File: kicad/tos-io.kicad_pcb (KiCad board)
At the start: 2 copper layers, 87.3 x 42.5 mm, 26 parts, among them J1 RaspPi Pin Header, J2 DE9_Receptacle, J3 Keyboard, J4 Mouse, J5 Conn_02x06_Odd_Even, SW1 STATUS, U1 MAX232

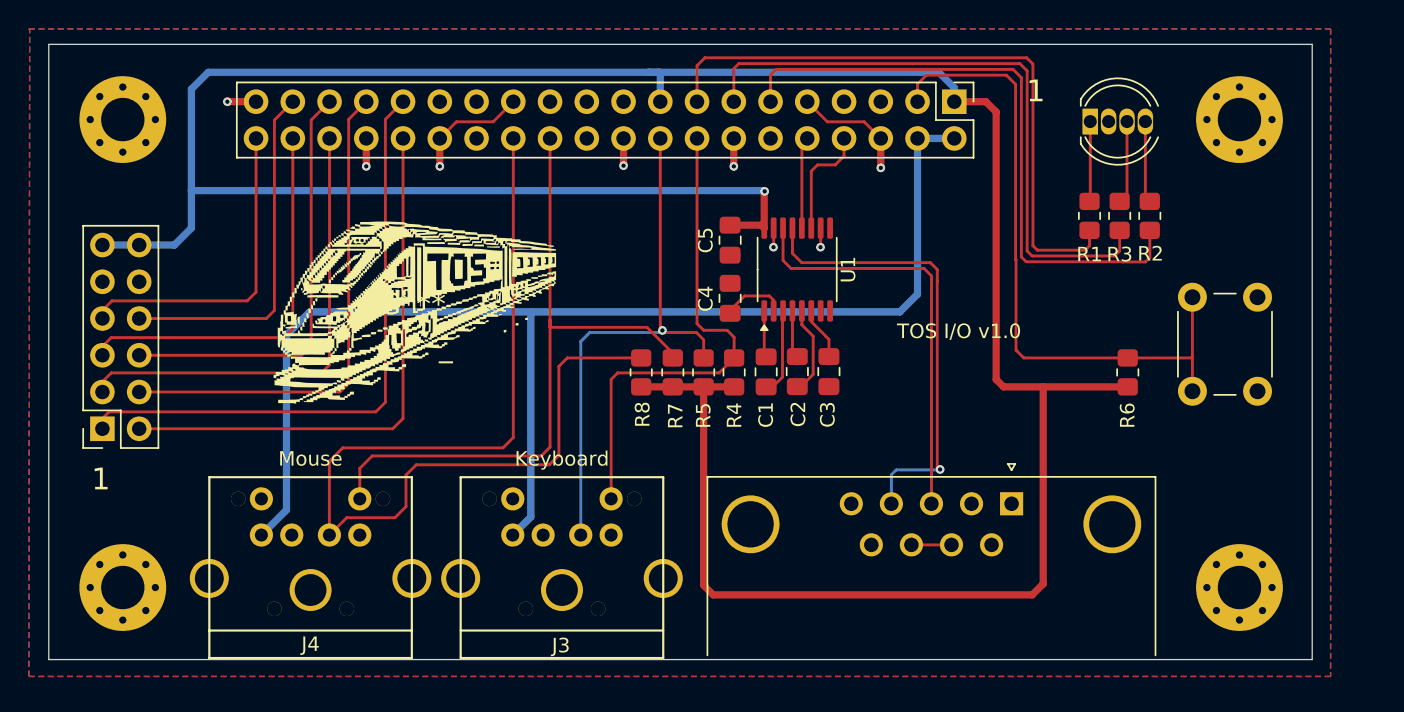
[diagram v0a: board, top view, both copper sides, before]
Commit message: Add breakout header on TOS I/O board
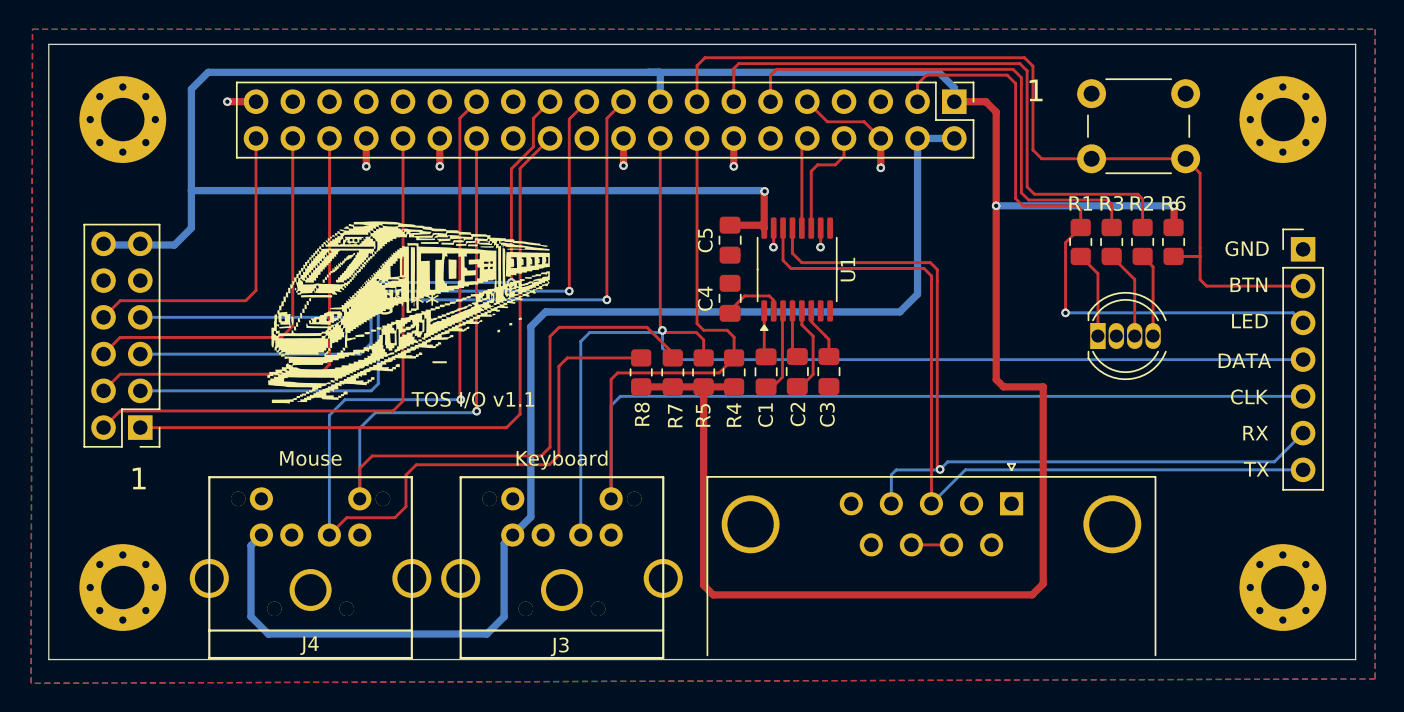
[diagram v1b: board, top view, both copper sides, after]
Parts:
- added J6: Conn_01x07, Connector_PinHeader_2.54mm:PinHeader_1x07_P2.54mm_Vertical, F.Cu at (177.1, 74.0)
- J5: value Conn_02x06_Odd_Even -> PMOD SPI 2A; footprint Connector_PinSocket_2.54mm:PinSocket_2x06_P2.54mm_Vertical -> Library:PinSocket_2x06_Top_Bottom_P2.54mm_Vertical
- moved SW1 18.2 mm to (162.5, 63.2), turned to 0 degrees
- moved D1 14.8 mm to (162.9, 80.0)
- moved R6 9.56 mm to (168.2, 73.5), turned to -90 degrees
- moved H3 3.00 mm to (175.7, 97.4)
- moved H4 3.00 mm to (175.7, 65.0)
- moved R1 1.90 mm to (161.8, 73.5), turned to -90 degrees
- moved R3 1.89 mm to (163.9, 73.5), turned to -90 degrees
- moved R2 1.87 mm to (166.0, 73.5), turned to -90 degrees
- moved G*** 0.43 mm to (115.1, 77.8)
- moved J5 0.39 mm to (93.8, 86.3)
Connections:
- net GPIO_14 renamed TXTTL
- net GPIO_15 renamed RXTTL
- net GPIO_23 renamed PS2_CLK
- net GPIO_24 renamed PS2_DATA
- J1 pad 11: GPIO_17 -> LED_BLUE
- J1 pad 13: GPIO_27 -> LED_GREEN
- J1 pad 15: GPIO_22 -> BUTTON
- J1 pad 19: unconnected-(J1-Pin_19-Pad19) -> PMOD_2_MOSI
- J1 pad 21: unconnected-(J1-Pin_21-Pad21) -> PMOD_3_MISO
- J1 pad 23: unconnected-(J1-Pin_23-Pad23) -> PMOD_4_SCK
- J1 pad 24: GPIO_8 -> PMOD_1_SS
- J1 pad 27: unconnected-(J1-Pin_27-Pad27) -> PS2_MOUSE_DATA
- J1 pad 28: unconnected-(J1-Pin_28-Pad28) -> PS2_MOUSE_CLK
- J1 pad 3: GPIO_2 -> LED_RED
- J1 pad 31: GPIO_6 -> unconnected-(J1-Pin_31-Pad31)
- J1 pad 32: GPIO_12 -> PMOD_7_INT
- J1 pad 33: GPIO_13 -> unconnected-(J1-Pin_33-Pad33)
- J1 pad 35: GPIO_19 -> unconnected-(J1-Pin_35-Pad35)
- J1 pad 36: GPIO_16 -> PMOD_8_RESET
- J1 pad 37: GPIO_26 -> unconnected-(J1-Pin_37-Pad37)
- J1 pad 38: GPIO_20 -> PMOD_9
- J1 pad 40: GPIO_21 -> PMOD_10
- J4 pad 1: GPIO_7 -> PS2_MOUSE_DATA
- J4 pad 5: GPIO_8 -> PS2_MOUSE_CLK
- J5 pad 1: GPIO_6 -> PMOD_1_SS
- J5 pad 10: GND -> PMOD_10
- J5 pad 11: +3V3 -> GND
- J5 pad 2: GPIO_12 -> PMOD_2_MOSI
- J5 pad 3: GPIO_16 -> PMOD_3_MISO
- J5 pad 4: GPIO_13 -> PMOD_4_SCK
- J5 pad 5: GPIO_20 -> GND
- J5 pad 6: GPIO_19 -> +3V3
- J5 pad 7: GPIO_21 -> PMOD_7_INT
- J5 pad 8: GPIO_26 -> PMOD_8_RESET
- J5 pad 9: GND -> PMOD_9
- R1 pad 1: GPIO_22 -> LED_RED
- R2 pad 1: GPIO_17 -> LED_GREEN
- R3 pad 1: GPIO_27 -> LED_BLUE
- R6 pad 2: GPIO_2 -> BUTTON
- R7 pad 1: GPIO_8 -> PS2_MOUSE_CLK
- R8 pad 1: GPIO_7 -> PS2_MOUSE_DATA
- SW1 pad 2: GPIO_2 -> BUTTON
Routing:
- net GPIO_7: track 70.7 -> 0.00 mm
- net PS2_MOUSE_DATA: track 0.00 -> 70.4 mm, vias 0 -> 1
- net PS2_MOUSE_CLK: track 0.00 -> 65.6 mm, vias 0 -> 1
- net BUTTON: track 0.00 -> 60.7 mm
- net PS2_CLK: track 34.6 -> 89.1 mm
- net PMOD_2_MOSI: track 0.00 -> 52.0 mm, vias 0 -> 1
- net GPIO_8: track 47.3 -> 0.00 mm
- net PMOD_3_MISO: track 0.00 -> 46.7 mm, vias 0 -> 1
- net PMOD_1_SS: track 0.00 -> 46.5 mm
- net GPIO_2: track 45.8 -> 0.00 mm
- net PS2_DATA: track 37.2 -> 83.0 mm
- net LED_RED: track 0.00 -> 45.5 mm, vias 0 -> 1
- net GPIO_22: track 43.9 -> 0.00 mm
- net GPIO_27: track 43.5 -> 0.00 mm
- net GPIO_17: track 43.0 -> 0.00 mm
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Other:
- board size 87.3 x 42.5 mm -> 90.3 x 42.5 mm
- board text added: "BTN"
- board text added: "CLK"
- board text added: "DATA"
- board text added: "GND"
- board text added: "LED"
- board text added: "RX"
- board text added: "TOS I/O v1.1"
- board text added: "TX"
- board text removed: "TOS I/O v1.0"
